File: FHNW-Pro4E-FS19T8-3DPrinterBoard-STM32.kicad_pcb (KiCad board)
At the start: 2 copper layers, 122 parts, among them J201 Micro_SD_Card_Det, J202 Conn_02x05_Counter_Clockwise, J203 Conn_02x05_Counter_Clockwise, J204 Conn_ARM_JTAG_SWD_20, J501 Conn_01x04, J502 USB_B_Mini, J503 Conn_01x04, J601 Conn_01x04, J602 Conn_01x04, J603 Conn_01x04, J604 Conn_01x04, Q301 2N3904, Q302 2N3904, SW201 SW_Push, T401 BUK963R3-60E, T402 BUK963R3-60E, T403 BUK963R3-60E, U101 LM2675M-3.3, U201 STM32F103ZETx, U301 ESP32-WROOM-32, U501 FT232RL, U601 TMC2660, U602 TMC2660, U603 TMC2660, U604 TMC2660, Y201 Crystal_8MHZ

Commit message: started layouting TMC2660
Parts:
- removed the R403 at (150.7, 103.4)
- removed the R605 at (116.8, 102.4)
- added C501: 10n, Capacitors_SMD:C_0603, F.Cu at (252.2, 47.6)
- added C502: 100n, Capacitors_SMD:C_0603, F.Cu at (252.2, 50.0)
- added C503: 4.7u, Capacitor_SMD:CP_Elec_6.3x5.3, F.Cu at (245.0, 47.6)
- added C504: 100n, Capacitors_SMD:C_0603, F.Cu at (256.1, 47.6)
- added C633: 470u, Capacitors_SMD:CP_Elec_6.3x5.3, F.Cu at (103.5, 144.8)
- added C634: 470u, Capacitors_SMD:CP_Elec_6.3x5.3, F.Cu at (40.0, 144.8)
- added C635: 470u, Capacitors_SMD:CP_Elec_6.3x5.3, F.Cu at (71.8, 144.8)
- added C636: 470u, Capacitors_SMD:CP_Elec_6.3x5.3, F.Cu at (135.3, 144.8)
- added J205: Conn_02x03_ISP, Connector_PinHeader_2.54mm:PinHeader_2x03_P2.54mm_Vertical, F.Cu at (242.0, 59.3)
- added L502: Ferrite_Bead, Resistors_SMD:R_0805_HandSoldering, F.Cu at (253.2, 45.0)
- added R408: nc, Resistors_SMD:R_0603, F.Cu at (154.6, 68.3)
- added R609: 10R, Resistors_SMD:R_0603, F.Cu at (71.1, 166.4)
- C101, C102, C103, C201, C202, C203, C204, C205, C206, C207, C208, C209, C210, C211, C401, C402, C403, C404, C405, C406, C601, C604, C607, C608, C609, C610, C611, C612, C613, C614, C615, C616, C617, C620, C623, C624, C625, C626, C627, C628, C629, C630, C631, C632: footprint Capacitors_SMD:C_0805 -> Capacitors_SMD:C_0603
- C602, C603, C605, C606, C618, C619, C621, C622: footprint Capacitors_SMD:C_0805 -> Capacitors_SMD:C_1210
- J601, J602, J603, J604: value Conn_01x04 -> B4B-XH-A; footprint Connector_PinHeader_2.54mm:PinHeader_1x04_P2.54mm_Vertical -> Connector_JST:JST_XH_B4B-XH-A_1x04_P2.50mm_Vertical
- R201, R202, R203, R204, R205, R206, R301, R302, R303, R401, R402, R404, R405, R406, R407, R409, R410, R411, R412, R501, R502, R503, R601, R603, R607, R611, R613, R615: footprint Resistors_SMD:R_0805 -> Resistors_SMD:R_0603
- R403: renamed from R408; footprint Resistors_SMD:R_0805 -> Resistors_SMD:R_0603
- R602, R604, R606, R608, R610, R612, R614, R616: footprint Resistors_SMD:R_0805 -> Resistors_SMD:R_1210
- R605: renamed from R609; footprint Resistors_SMD:R_0805 -> Resistors_SMD:R_0603
- moved C612 105.3 mm to (50.8, 168.3), turned to 180 degrees
- moved J602 103.3 mm to (48.9, 175.3), turned to 180 degrees
- moved R603 99.4 mm to (39.4, 166.4)
- moved J604 98.3 mm to (144.1, 175.3), turned to 180 degrees
- moved C616 98.1 mm to (40.6, 170.2), turned to 180 degrees
- moved U604 97.5 mm to (140.3, 158.8)
- moved J603 94.3 mm to (80.6, 175.3), turned to 180 degrees
- moved C615 92.8 mm to (44.5, 149.2)
- moved J601 91.5 mm to (112.4, 175.3), turned to 180 degrees
- moved C610 89.3 mm to (39.4, 168.3)
- moved C632 86.5 mm to (135.9, 170.2), turned to 180 degrees
- moved C628 82.0 mm to (146.1, 168.3), turned to 180 degrees
- moved C630 81.9 mm to (72.4, 170.2), turned to 180 degrees
- moved C626 81.7 mm to (134.5, 168.3)
- moved R610 81.3 mm to (67.3, 163.8), turned to 90 degrees
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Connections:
- J502 pad 1: +5V -> Net-(C501-Pad1)
- J601 pad 1: Net-(J601-Pad1) -> /appendix_TMC2660_X/MOT_Y_B1
- J601 pad 2: Net-(J601-Pad2) -> /appendix_TMC2660_X/MOT_Y_B2
- J601 pad 3: Net-(J601-Pad3) -> /appendix_TMC2660_X/MOT_Y_A2
- J601 pad 4: Net-(J601-Pad4) -> /appendix_TMC2660_X/MOT_Y_A1
- J602 pad 1: Net-(J602-Pad1) -> /appendix_TMC2660_X/MOT_X_B1
- J602 pad 2: Net-(J602-Pad2) -> /appendix_TMC2660_X/MOT_X_B2
- J602 pad 3: Net-(J602-Pad3) -> /appendix_TMC2660_X/MOT_X_A2
- J602 pad 4: Net-(J602-Pad4) -> /appendix_TMC2660_X/MOT_X_A1
- J603 pad 1: Net-(J603-Pad1) -> /appendix_TMC2660_X/MOT_E1_B1
- J603 pad 2: Net-(J603-Pad2) -> /appendix_TMC2660_X/MOT_E1_B2
- J603 pad 3: Net-(J603-Pad3) -> /appendix_TMC2660_X/MOT_E1_A2
- J603 pad 4: Net-(J603-Pad4) -> /appendix_TMC2660_X/MOT_E1_A1
- J604 pad 1: Net-(J604-Pad1) -> /appendix_TMC2660_X/MOT_Z1_B1
- J604 pad 2: Net-(J604-Pad2) -> /appendix_TMC2660_X/MOT_Z1_B2
- J604 pad 3: Net-(J604-Pad3) -> /appendix_TMC2660_X/MOT_Z1_A2
- J604 pad 4: Net-(J604-Pad4) -> /appendix_TMC2660_X/MOT_Z1_A1
- R403 pad 1: /appendix_SENSORS_POWER/SW_End_Y_min -> /appendix_SENSORS_POWER/SW_End_X_min
- R501 pad 1: +5V -> V_USB
- R502 pad 1: +3V3 -> /appendix_UART_USB/USB_VCCIO_3.3V
- R605 pad 1: Net-(R609-Pad1) -> Net-(R605-Pad1)
- R605 pad 2: Net-(C625-Pad2) -> Net-(C611-Pad2)
- U501 pad 17: Net-(U501-Pad17) -> /appendix_UART_USB/USB_VCCIO_3.3V
- U501 pad 20: +5V -> V_USB
- U501 pad 4: +3V3 -> /appendix_UART_USB/USB_VCCIO_3.3V
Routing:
- net GND: track 0.00 -> 111.8 mm, vias 0 -> 35
- net /appendix_TMC2660_X/MOT_X_B1: track 0.00 -> 55.8 mm, vias 0 -> 13
- net /appendix_TMC2660_X/MOT_X_B2: track 0.00 -> 51.1 mm, vias 0 -> 14
- net /appendix_TMC2660_X/D_SPI_MISO: track 0.00 -> 48.4 mm, vias 0 -> 5
- net /appendix_TMC2660_X/D_SPI_SCK: track 0.00 -> 46.5 mm, vias 0 -> 5
- net /appendix_TMC2660_X/D_SPI_MOSI: track 0.00 -> 37.6 mm, vias 0 -> 5
- net /appendix_TMC2660_X/MOT_X_A2: track 0.00 -> 34.5 mm, vias 0 -> 6
- net /appendix_TMC2660_X/D_TMC_EN_X: track 0.00 -> 32.4 mm, vias 0 -> 2
- net /appendix_TMC2660_X/MOT_X_A1: track 0.00 -> 28.9 mm, vias 0 -> 5
- net +12V: track 0.00 -> 26.6 mm
- net /appendix_TMC2660_X/D_TMC_DIR_X: track 0.00 -> 12.2 mm, vias 0 -> 2
- net Net-(C615-Pad1): track 0.00 -> 11.7 mm, vias 0 -> 2
- net Net-(C616-Pad1): track 0.00 -> 9.86 mm
- net Net-(R607-Pad1): track 0.00 -> 9.31 mm
- net Net-(C610-Pad2): track 0.00 -> 9.01 mm
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- added copper zone on F.Cu, net (none)
- added copper zone on F.Cu, net +12V
- added copper zone on B.Cu, net /appendix_TMC2660_X/MOT_X_A1
- added copper zone on F.Cu, net /appendix_TMC2660_X/MOT_X_A1
- added copper zone on B.Cu, net /appendix_TMC2660_X/MOT_X_A2
- added copper zone on F.Cu, net /appendix_TMC2660_X/MOT_X_A2
- added copper zone on B.Cu, net /appendix_TMC2660_X/MOT_X_B1
- added copper zone on F.Cu, net /appendix_TMC2660_X/MOT_X_B1
- added copper zone on B.Cu, net /appendix_TMC2660_X/MOT_X_B2
- added copper zone on F.Cu, net /appendix_TMC2660_X/MOT_X_B2
- added copper zone on F.Cu, net GND
- added copper zone on In1.Cu, net GND
- added copper zone on F.Cu, net Net-(R603-Pad1)
- added copper zone on F.Cu, net Net-(R607-Pad1)
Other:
- copper layers 2 -> 4
- net class Default: trace_width 0.25 -> 0.5; via_dia 0.8 -> 1; via_drill 0.4 -> 0.5
- net class Stepper Motors added: clearance 0.2, trace_width 1.2, via_dia 1, via_drill 0.5

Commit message: Layout: all TMC / Schematic: Oli's comments
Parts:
- moved U201 144.4 mm to (179.1, 50.8)
- moved C618 111.3 mm to (175.9, 86.4)
- moved C619 111.3 mm to (160.7, 86.4)
- moved C627 111.3 mm to (174.0, 104.8)
- moved C630 111.3 mm to (163.8, 106.7)
- moved J603 111.3 mm to (172.1, 111.8)
- moved R610 111.3 mm to (158.8, 100.3)
- moved R613 111.3 mm to (174.0, 102.9)
- moved R614 111.3 mm to (177.8, 100.3)
- moved U603 111.3 mm to (168.3, 95.2)
- moved C617 111.3 mm to (171.4, 84.5)
- moved C625 111.3 mm to (162.6, 104.8)
- moved C635 111.3 mm to (163.2, 81.3)
- moved R609 111.3 mm to (162.6, 102.9)
- moved C623 111.3 mm to (171.4, 87.0)
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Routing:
- net GND: track 111.8 -> 52.7 mm, vias 35 -> 48
- net /appendix_TMC2660_X/MOT_X_B1: track 55.8 -> 18.7 mm, vias 13 -> 6
- net /appendix_TMC2660_X/MOT_X_B2: track 51.1 -> 16.5 mm, vias 14 -> 6
- net /appendix_TMC2660_X/D_TMC_CS_X: track 5.21 -> 32.3 mm
- net /appendix_TMC2660_X/D_SPI_SCK: track 46.5 -> 20.3 mm, vias 5 -> 4
- net /appendix_TMC2660_X/D_SPI_MISO: track 48.4 -> 23.8 mm, vias 5 -> 4
- net /appendix_TMC2660_X/D_SPI_MOSI: track 37.6 -> 13.1 mm, vias 5 -> 4
- net /appendix_TMC2660_X/MOT_X_A2: track 34.5 -> 16.5 mm
- net /appendix_TMC2660_X/MOT_Y_A2: track 0.00 -> 16.5 mm, vias 0 -> 6
- net /appendix_TMC2660_X/MOT_Z1_A2: track 0.00 -> 16.5 mm, vias 0 -> 6
- net /appendix_TMC2660_X/MOT_E1_A2: track 0.00 -> 16.5 mm, vias 0 -> 6
- net /appendix_TMC2660_X/MOT_Z1_B2: track 0.00 -> 16.5 mm, vias 0 -> 6
- net /appendix_TMC2660_X/MOT_Y_B2: track 0.00 -> 16.5 mm, vias 0 -> 6
- net /appendix_TMC2660_X/MOT_E1_B2: track 0.00 -> 16.5 mm, vias 0 -> 6
- net /appendix_TMC2660_X/MOT_Z1_A1: track 0.00 -> 13.5 mm, vias 0 -> 6
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- added copper zone on B.Cu, net /appendix_TMC2660_X/MOT_E1_A1
- added copper zone on F.Cu, net /appendix_TMC2660_X/MOT_E1_A1
- added copper zone on B.Cu, net /appendix_TMC2660_X/MOT_E1_A2
- added copper zone on F.Cu, net /appendix_TMC2660_X/MOT_E1_A2
- added copper zone on B.Cu, net /appendix_TMC2660_X/MOT_E1_B1
- added copper zone on F.Cu, net /appendix_TMC2660_X/MOT_E1_B1
- added copper zone on B.Cu, net /appendix_TMC2660_X/MOT_E1_B2
- added copper zone on F.Cu, net /appendix_TMC2660_X/MOT_E1_B2
- added copper zone on B.Cu, net /appendix_TMC2660_X/MOT_Y_A1
- added copper zone on F.Cu, net /appendix_TMC2660_X/MOT_Y_A1
- added copper zone on B.Cu, net /appendix_TMC2660_X/MOT_Y_A2
- added copper zone on F.Cu, net /appendix_TMC2660_X/MOT_Y_A2
- added copper zone on B.Cu, net /appendix_TMC2660_X/MOT_Y_B1
- added copper zone on F.Cu, net /appendix_TMC2660_X/MOT_Y_B1
- added copper zone on B.Cu, net /appendix_TMC2660_X/MOT_Y_B2
- added copper zone on F.Cu, net /appendix_TMC2660_X/MOT_Y_B2
- added copper zone on B.Cu, net /appendix_TMC2660_X/MOT_Z1_A1
- added copper zone on F.Cu, net /appendix_TMC2660_X/MOT_Z1_A1
- added copper zone on B.Cu, net /appendix_TMC2660_X/MOT_Z1_A2
- added copper zone on F.Cu, net /appendix_TMC2660_X/MOT_Z1_A2
- added copper zone on B.Cu, net /appendix_TMC2660_X/MOT_Z1_B1
- added copper zone on F.Cu, net /appendix_TMC2660_X/MOT_Z1_B1
- added copper zone on B.Cu, net /appendix_TMC2660_X/MOT_Z1_B2
- added copper zone on F.Cu, net /appendix_TMC2660_X/MOT_Z1_B2
- added copper zone on F.Cu, net Net-(R601-Pad1)
- added copper zone on F.Cu, net Net-(R605-Pad1)
- added copper zone on F.Cu, net Net-(R609-Pad1)
- added copper zone on F.Cu, net Net-(R611-Pad1)
- added copper zone on F.Cu, net Net-(R613-Pad1)
- added copper zone on F.Cu, net Net-(R615-Pad1)
- removed copper zone on F.Cu, net (none)
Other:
- board text added: "E"
- board text added: "E-Mot"
- board text added: "X"
- board text added: "X-Mot"
- board text added: "Y"
- board text added: "Y-Mot"
- board text added: "Z"
- board text added: "Z-Mot"

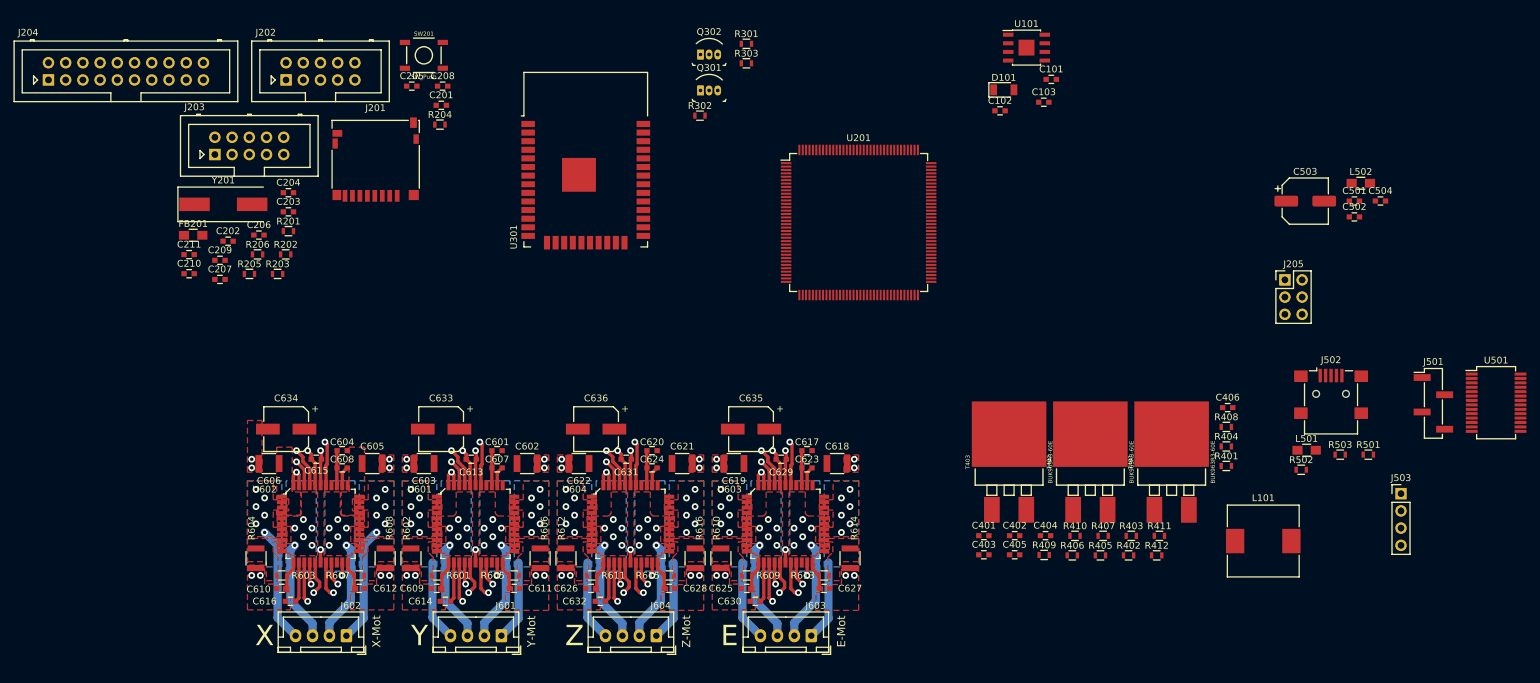
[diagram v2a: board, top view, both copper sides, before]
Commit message: added footprints, layouted 3v3 Reg
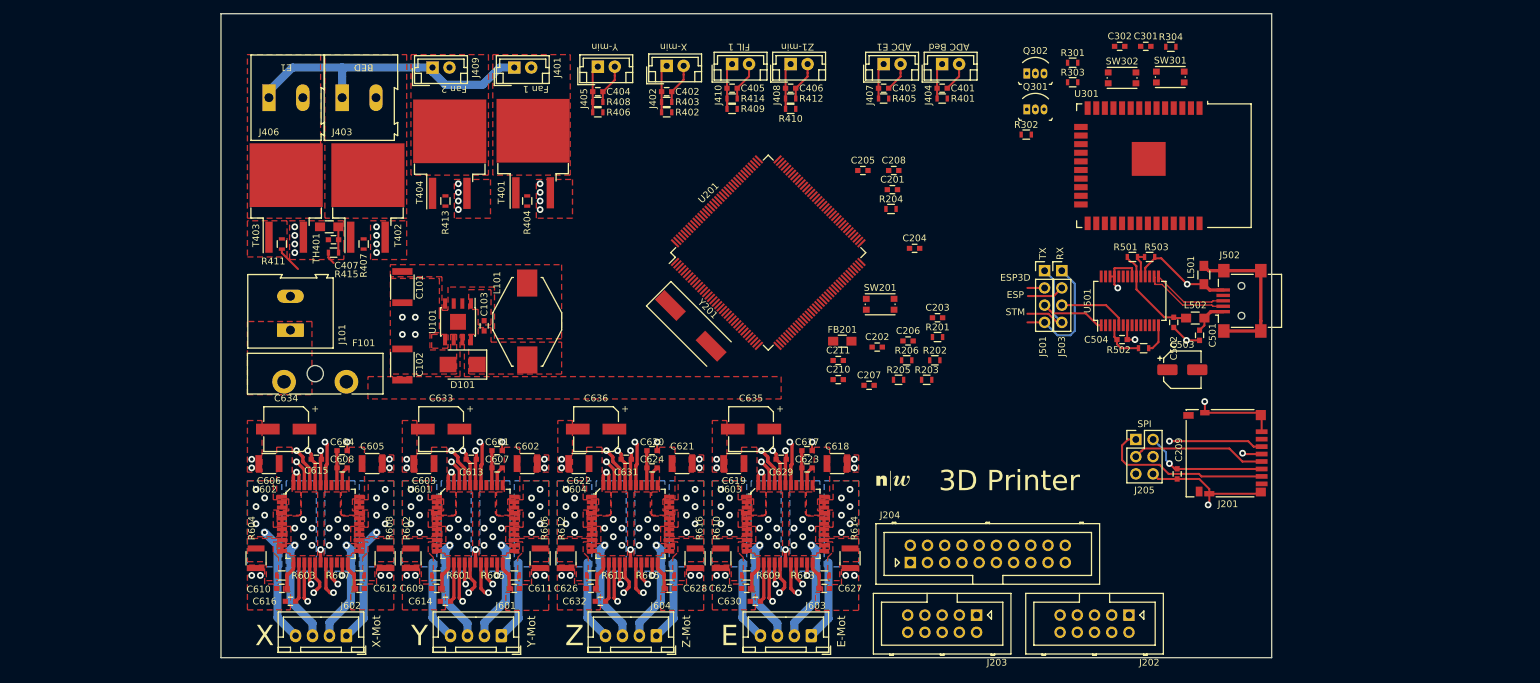
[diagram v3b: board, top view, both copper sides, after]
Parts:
- added C301: 100n, Capacitors_SMD:C_0603, F.Cu at (221.4, 24.8)
- added C302: 100n, Capacitors_SMD:C_0603, F.Cu at (217.6, 24.8)
- added C407: 10u, Capacitors_SMD:C_0603, F.Cu at (101.6, 53.3)
- added F101: Fuse, Fuse:Fuseholder_Blade_ATO_Littelfuse_Pudenz_2_Pin, F.Cu at (103.5, 74.3)
- added G***: Logo_FHNW_03x05mm, A_Tale_Of_A_Library:Logo_FHNW_03x05mm, F.Cu at (184.2, 88.9)
- added J101: Screw_Terminal_01x02, Connectors_Terminal_Blocks:TerminalBlock_Altech_AK300-2_P5.00mm, F.Cu at (95.2, 66.7)
- added J401: Conn_01x02, Connectors_JST:JST_EH_B02B-EH-A_02x2.50mm_Straight, F.Cu at (128.3, 27.9)
- added J402: Conn_01x02, Connectors_JST:JST_EH_B02B-EH-A_02x2.50mm_Straight, F.Cu at (150.7, 27.7)
- added J403: Screw_Terminal_01x02, Connectors_Terminal_Blocks:TerminalBlock_Altech_AK300-2_P5.00mm, F.Cu at (102.9, 32.4)
- added J404: Conn_01x02, Connectors_JST:JST_EH_B02B-EH-A_02x2.50mm_Straight, F.Cu at (191.4, 27.4)
- added J405: Conn_01x02, Connectors_JST:JST_EH_B02B-EH-A_02x2.50mm_Straight, F.Cu at (140.6, 27.8)
- added J406: Screw_Terminal_01x02, Connectors_Terminal_Blocks:TerminalBlock_Altech_AK300-2_P5.00mm, F.Cu at (92.1, 32.4)
- added J407: Conn_01x02, Connectors_JST:JST_EH_B02B-EH-A_02x2.50mm_Straight, F.Cu at (182.8, 27.4)
- added J408: Conn_01x02, Connectors_JST:JST_EH_B02B-EH-A_02x2.50mm_Straight, F.Cu at (169.0, 27.4)
- added J409: Conn_01x02, Connectors_JST:JST_EH_B02B-EH-A_02x2.50mm_Straight, F.Cu at (116.2, 27.9)
- added J410: Conn_01x02, Connectors_JST:JST_EH_B02B-EH-A_02x2.50mm_Straight, F.Cu at (160.4, 27.4)
- added R304: 10k, Resistors_SMD:R_0603, F.Cu at (225.1, 24.9)
- added R413: 10k, Resistors_SMD:R_0603, F.Cu at (118.1, 47.6)
- added R414: nc, Resistors_SMD:R_0603, F.Cu at (160.4, 32.5)
- added R415: 4k7, Resistors_SMD:R_0603, F.Cu at (101.6, 55.2)
- added SW301: SW_Push, Button_Switch_SMD:SW_SPST_KMR2, F.Cu at (225.0, 29.3)
- added SW302: SW_Push, Button_Switch_SMD:SW_SPST_KMR2, F.Cu at (217.9, 29.5)
- added T404: BUK963R3-60E, Package_TO_SOT_SMD:TO-263-2, F.Cu at (118.7, 40.7)
- added TH401: Thermistor_NTC, Resistors_SMD:R_0805_HandSoldering, F.Cu at (101.0, 51.4)
- C101, C102: footprint Capacitors_SMD:C_0603 -> Capacitors_SMD:C_1812
- C503: footprint Capacitor_SMD:CP_Elec_6.3x5.3 -> Capacitor_SMD:CP_Elec_5x5.9
- D101: footprint Diodes_SMD:D_1206 -> Diodes_SMD:D_SMB
- J204: value Conn_ARM_JTAG_SWD_20 -> Conn_ARM_JTAG_SWD_10
- J501: footprint Connector_PinHeader_2.54mm:PinHeader_1x04_P2.54mm_Vertical_SMD_Pin1Left -> Connector_PinHeader_2.54mm:PinHeader_1x04_P2.54mm_Vertical
- L101: footprint Inductors_SMD:L_10.4x10.4_H4.8 -> Inductors_SMD:L_Fastron_PISN_Handsoldering
- SW201: footprint Switches:TACTILE_SWITCH_SMD_5.2MM -> Button_Switch_SMD:SW_SPST_KMR2
- T401, T402, T403: footprint Silicon-Standard:TO-263_D2PAK -> Package_TO_SOT_SMD:TO-263-2
- moved J202 147.3 mm to (218.9, 108.7), turned to 180 degrees
- moved J204 145.7 mm to (186.7, 101.0)
- moved C209 144.7 mm to (226.1, 87.9), turned to 270 degrees
- moved R411 136.4 mm to (94.0, 54.0), turned to 270 degrees
- moved J201 132.6 mm to (233.2, 84.8), turned to 90 degrees
- moved J203 131.3 mm to (196.5, 108.7), turned to 180 degrees
- moved R407 117.3 mm to (106.0, 54.0), turned to 270 degrees
- moved T403 113.5 mm to (94.6, 47.2), turned to 90 degrees
- moved T402 113.5 mm to (106.7, 47.2), turned to 90 degrees
- moved L101 113.3 mm to (130.2, 65.4), turned to 270 degrees
- moved R404 109.3 mm to (130.2, 47.6), turned to 270 degrees
- moved T401 104.6 mm to (131.0, 40.6), turned to 90 degrees
- moved R408 104.4 mm to (140.6, 33.0)
- moved C101 100.5 mm to (111.8, 60.3), turned to 270 degrees
- moved FB201 97.0 mm to (176.7, 68.3)
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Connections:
- net +12V renamed +24V
- net /appendix_SENSORS_POWER/ADC_Temp_HotEnd renamed /appendix_SENSORS_POWER/ADC_Temp_E1
- net /appendix_SENSORS_POWER/DP_Hotend_1 renamed /appendix_SENSORS_POWER/DP_E1
- net /appendix_SENSORS_POWER/SW_End_Z_min renamed /appendix_SENSORS_POWER/SW_End_Z1_min
- net /appendix_UART_USB/USB_DM renamed /appendix_UART_USB/USB_D_N
- net /appendix_UART_USB/USB_DP renamed /appendix_UART_USB/USB_D_P
- net Net-(U601-Pad38) renamed /appendix_TMC2660_X/D_INT_TMC_STALL_Y
- net Net-(U602-Pad38) renamed /appendix_TMC2660_X/D_INT_TMC_STALL_X
- net Net-(U603-Pad38) renamed /appendix_TMC2660_X/D_INT_TMC_STALL_E1
- net Net-(U604-Pad38) renamed /appendix_TMC2660_X/D_INT_TMC_STALL_Z1
- C613 pad 1: Net-(C613-Pad1) -> +3V3
- C615 pad 1: Net-(C615-Pad1) -> +3V3
- C629 pad 1: Net-(C629-Pad1) -> +3V3
- C631 pad 1: Net-(C631-Pad1) -> +3V3
- J204 pad 10: GND -> JTAG_RESET
- J204 pad 11: Net-(J204-Pad11) -> (no net)
- J204 pad 12: GND -> (no net)
- J204 pad 13: JTAG_TDO_SWO -> (no net)
- J204 pad 14: GND -> (no net)
- J204 pad 15: JTAG_RESET -> (no net)
- J204 pad 16: GND -> (no net)
- J204 pad 17: Net-(J204-Pad17) -> (no net)
- J204 pad 18: GND -> (no net)
- J204 pad 19: Net-(J204-Pad19) -> (no net)
- J204 pad 2: +3V3 -> JTAG_TMS_SWDIO
- J204 pad 20: GND -> (no net)
- J204 pad 3: JTAG_TRST -> GND
- J204 pad 4: GND -> JTAG_TCK_SWCLK
- J204 pad 5: JTAG_TDI -> GND
- J204 pad 6: GND -> JTAG_TDO_SWO
- J204 pad 7: JTAG_TMS_SWDIO -> Net-(J204-Pad7)
- J204 pad 8: GND -> JTAG_TDI
- J204 pad 9: JTAG_TCK_SWCLK -> GND
- J205 pad 5: JTAG_RESET -> Net-(J205-Pad5)
- T401 pad 2: Net-(T401-Pad2) -> /appendix_SENSORS_POWER/Fan1_pwr
- T402 pad 2: Net-(T402-Pad2) -> /appendix_SENSORS_POWER/Bed_pwr
- T403 pad 2: Net-(T403-Pad2) -> /appendix_SENSORS_POWER/E1_pwr
- U601 pad 40: Net-(C613-Pad1) -> +3V3
- U602 pad 40: Net-(C615-Pad1) -> +3V3
- U603 pad 40: Net-(C629-Pad1) -> +3V3
- U604 pad 40: Net-(C631-Pad1) -> +3V3
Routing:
- net GND: track 52.7 -> 155.7 mm, vias 48 -> 79
- net /appendix_TMC2660_X/D_SPI_MOSI: track 13.1 -> 86.9 mm
- net /appendix_TMC2660_X/D_SPI_SCK: track 20.3 -> 92.4 mm
- net /appendix_TMC2660_X/D_SPI_MISO: track 23.8 -> 93.8 mm
- net +24V: track 20.4 -> 66.0 mm
- net +3V3: track 0.00 -> 42.5 mm, vias 0 -> 5
- net /appendix_STM32F103/D_SPI_MISO: track 0.00 -> 26.2 mm
- net Net-(J502-Pad6): track 0.00 -> 23.0 mm
- net /appendix_STM32F103/D_SPI_SCK: track 0.00 -> 19.8 mm
- net /appendix_UART_USB/D_TX_to_STM_RX: track 0.00 -> 17.7 mm
- net /appendix_STM32F103/D_SPI_MOSI: track 0.00 -> 17.3 mm, vias 0 -> 1
- net V_USB: track 0.00 -> 14.5 mm
- net /appendix_UART_USB/D_RX_to_STM_TX: track 0.00 -> 14.3 mm
- net /appendix_UART_USB/USB_D_N: track 0.00 -> 12.6 mm
- net /appendix_UART_USB/USB_D_P: track 0.00 -> 11.2 mm
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- added copper zone on F.Cu, net +3V3
- added copper zone on F.Cu, net /appendix_SENSORS_POWER/Bed_pwr
- added copper zone on F.Cu, net /appendix_SENSORS_POWER/E1_pwr
- added copper zone on F.Cu, net /appendix_SENSORS_POWER/Fan1_pwr
- added copper zone on F.Cu, net /appendix_SENSORS_POWER/Fan2_pwr
- added copper zone on F.Cu, net Net-(C103-Pad1)
- added copper zone on F.Cu, net Net-(C103-Pad2)
- added copper zone on F.Cu, net Net-(F101-Pad2)
- added copper zone on F.Cu, net Net-(R411-Pad1)
- added copper zone on F.Cu, net Net-(U101-Pad5)
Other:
- board outline added: 155 x 95 mm
- net class Default: trace_width 0.5 -> 0.3
- net class thick added: clearance 0.2, trace_width 1.2, via_dia 1.4, via_drill 1
- board text added: "3D Printer"
- board text added: "ADC Bed"
- board text added: "ADC E1"
- board text added: "BED"
- board text added: "E1"
- board text added: "ESP"
- board text added: "ESP3D"
- board text added: "FIL 1"
- board text added: "Fan 1"
- board text added: "Fan 2"
- board text added: "RX"
- board text added: "SPI"
- board text added: "STM"
- board text added: "TX"
- board text added: "X-min"
- board text added: "Y-min"
- board text added: "Z1-min"
